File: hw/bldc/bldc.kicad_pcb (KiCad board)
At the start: 2 copper layers, 54 x 29 mm, 71 parts, among them IC1 MP2315SGJ-P, J1 Conn_01x05, J3 Conn_01x06, Q1 BSC13DN30NSFD, Q10 BSC13DN30NSFD, Q2 BSC13DN30NSFD, Q7 BSC13DN30NSFD, Q8 BSC13DN30NSFD, Q9 BSC13DN30NSFD, U1 LD1117S33TR_SOT223, U2 IR2101, U3 IR2101, U4 IR2101, U5 STM32L431CCTx

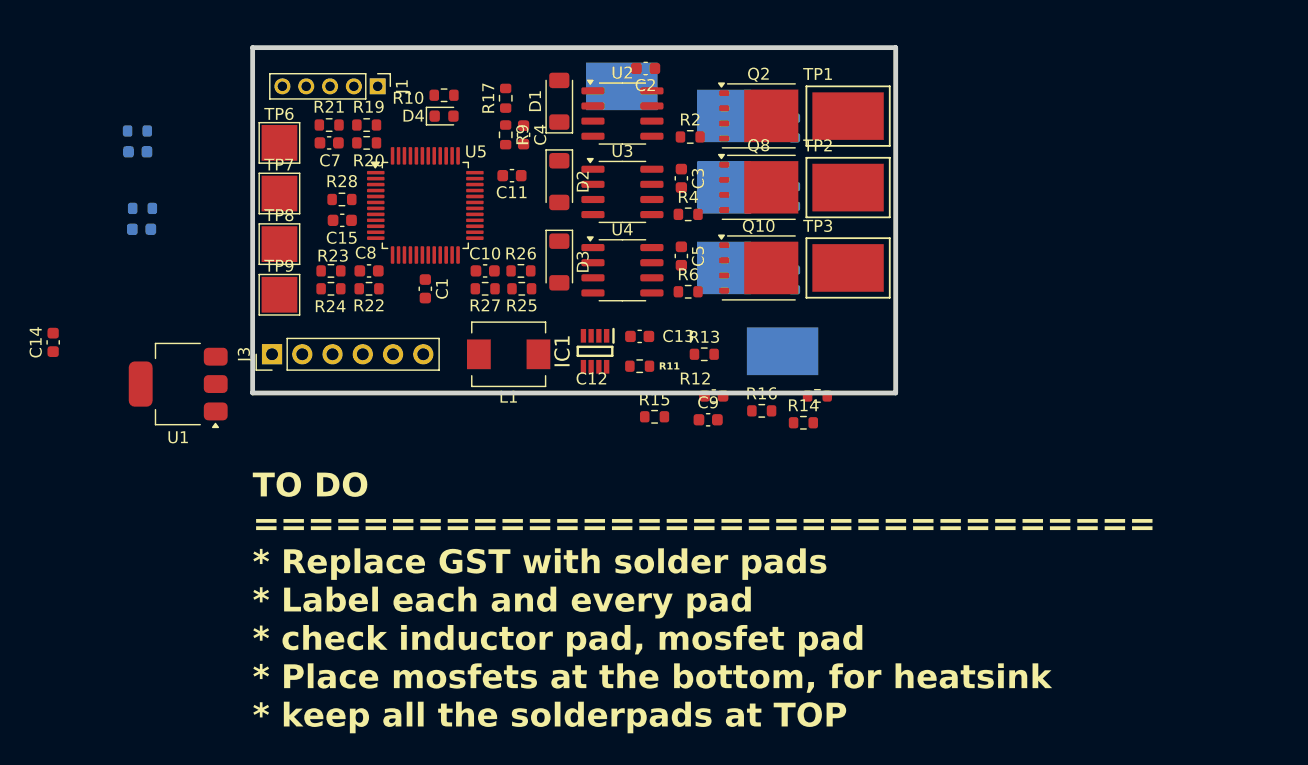
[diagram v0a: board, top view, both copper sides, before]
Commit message: component placement
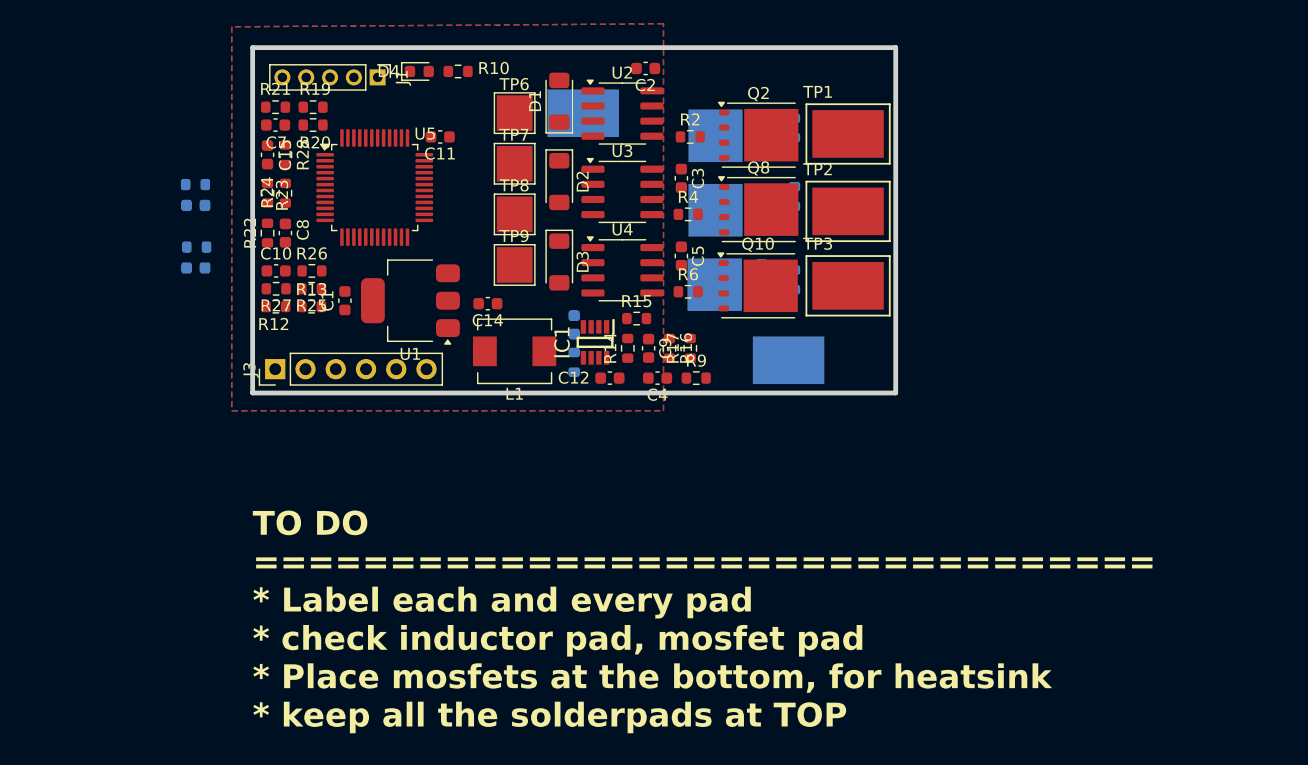
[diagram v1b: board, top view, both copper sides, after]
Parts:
- C13, R11: moved to B.Cu
- C14: value 0.1uF -> 10uF
- moved R12 46.1 mm to (52.0, 117.8)
- moved C14 36.6 mm to (69.8, 117.5), turned to 180 degrees
- moved R13 33.2 mm to (55.0, 117.8)
- moved R17 26.1 mm to (86.8, 121.2)
- moved R9 25.9 mm to (87.2, 123.8), turned to 0 degrees
- moved C4 23.3 mm to (84.0, 123.8), turned to 180 degrees
- moved U1 20.7 mm to (63.2, 117.2)
- moved TP6 19.9 mm to (72.0, 101.5)
- moved TP7 19.9 mm to (72.0, 105.8)
- moved TP8 19.9 mm to (72.0, 110.0)
- moved TP9 19.9 mm to (72.0, 114.2)
- moved R25 17.6 mm to (55.0, 116.2)
- moved C10 17.6 mm to (52.0, 114.8)
- moved R26 17.6 mm to (55.0, 114.8)
- moved R27 17.6 mm to (52.0, 116.2)
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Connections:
- R16 pad 1: VDD -> VDC
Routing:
- added copper zone on B.Cu, net GND
- added copper zone on F.Cu, net GND
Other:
- board text added: "TO DO ================================= * Label each and every pad * check inductor pad, mosfet pad * Place mosfets at the bottom, for heatsink * keep all the solderpads at TOP"
- board text removed: "TO DO ================================= * Replace GST with solder pads * Label each and every pad * check inductor pad, mosfet pad * Place mosfets at the bottom, for heatsink * keep all the solderpads at TOP"

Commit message: pcb routing update
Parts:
- D1, D2, D3: moved to B.Cu
- moved R12 20.6 mm to (72.5, 117.5)
- moved R13 20.6 mm to (75.5, 117.5)
- moved D1 6.05 mm to (81.0, 97.5), turned to 180 degrees
- moved C16 5.52 mm to (45.7, 103.8)
- moved C17 5.52 mm to (45.7, 109.0)
- moved R18 5.52 mm to (45.8, 107.2)
- moved R7 5.52 mm to (45.7, 102.0)
- moved D2 5.30 mm to (81.0, 106.5), turned to 180 degrees
- moved D3 5.30 mm to (81.0, 113.2), turned to 180 degrees
- moved C13 4.49 mm to (74.5, 123.0), turned to 180 degrees
- moved C2 4.07 mm to (85.8, 100.8), turned to -90 degrees
- moved R3 3.26 mm to (95.2, 111.8), turned to 180 degrees
- moved TP6 3.25 mm to (72.0, 98.2)
- moved R1 2.76 mm to (95.2, 105.5), turned to 180 degrees
- moved R5 2.25 mm to (95.5, 117.8), turned to 180 degrees
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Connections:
- U2 pad 2: /TIM1_CH1 -> /TIM1_CH3
- U2 pad 3: /TIM1_CH1N -> /TIM1_CH3N
- U4 pad 2: /TIM1_CH3 -> /TIM1_CH1
- U4 pad 3: /TIM1_CH3N -> /TIM1_CH1N
- U5 pad 28: /LED -> unconnected-(U5-PB15-Pad28)
- U5 pad 32: unconnected-(U5-PA11-Pad32) -> /LED
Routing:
- net +3V3: track 0.00 -> 69.6 mm, vias 0 -> 4
- net /PHASE_A: track 0.00 -> 62.6 mm, vias 0 -> 11
- net /PHASE_B: track 0.00 -> 53.7 mm, vias 0 -> 10
- net /PHASE_C: track 0.00 -> 52.8 mm, vias 0 -> 11
- net VDD: track 0.00 -> 51.7 mm, vias 0 -> 4
- net /ADC_VDC: track 0.00 -> 40.6 mm, vias 0 -> 2
- net /TIM1_CH3N: track 0.00 -> 27.6 mm, vias 0 -> 2
- net /ADC_CENTER: track 0.00 -> 26.5 mm, vias 0 -> 4
- net Net-(U4-HO): track 0.00 -> 23.2 mm, vias 0 -> 1
- net /TIM1_CH2N: track 0.00 -> 22.8 mm, vias 0 -> 2
- net /MCU_TX: track 0.00 -> 22.4 mm, vias 0 -> 1
- net Net-(U3-HO): track 0.00 -> 22.2 mm, vias 0 -> 1
- net /TIM1_CH1N: track 0.00 -> 22.0 mm
- net /MCU_RX: track 0.00 -> 22.0 mm, vias 0 -> 1
- net Net-(U2-HO): track 0.00 -> 21.6 mm, vias 0 -> 1
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- added copper zone on B.Cu, net /PHASE_A
- added copper zone on F.Cu, net /PHASE_A
- added copper zone on B.Cu, net /PHASE_B
- added copper zone on F.Cu, net /PHASE_B
- added copper zone on B.Cu, net /PHASE_C
- added copper zone on F.Cu, net /PHASE_C
- added copper zone on B.Cu, net VDC

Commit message: PCB update
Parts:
- moved C17 29.9 mm to (75.5, 106.5), turned to -90 degrees
- moved R7 21.8 mm to (67.2, 105.5), turned to 0 degrees
- moved R18 21.7 mm to (67.2, 104.0), turned to 0 degrees
- moved C16 21.6 mm to (67.2, 102.5)
- moved R6 1.52 mm to (86.8, 118.0)
- moved R4 0.75 mm to (86.5, 110.8)
- moved C3 0.50 mm to (85.8, 107.0)
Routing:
- net GND: track 15.4 -> 81.9 mm, vias 12 -> 22
- net /ADC_SPD: track 0.00 -> 13.6 mm, vias 0 -> 1
- net Net-(C17-Pad2): track 0.00 -> 12.8 mm, vias 0 -> 1
- net Net-(R18-Pad2): track 0.00 -> 4.13 mm, vias 0 -> 1
- net /ADC_CENTER: track 26.5 -> 30.4 mm
- net /PHASE_B: track 53.7 -> 57.7 mm, vias 10 -> 13
- net Net-(Q10-G): track 3.29 -> 2.01 mm
- net Net-(U4-LO): track 2.19 -> 2.98 mm
- net Net-(Q8-G): track 3.35 -> 2.63 mm

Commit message: PCB UPDATE
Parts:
- moved TP4 1.50 mm to (93.5, 122.2)
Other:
- board size 54 x 29 mm -> 54 x 29.2 mm
- board text added: "3.3V"
- board text added: "GND"
- board text added: "LED"
- board text added: "PHASE A"
- board text added: "PHASE B"
- board text added: "PHASE C"
- board text added: "RPM"
- board text added: "RX"
- board text added: "SPD"
- board text added: "TX"
- board text added: "VCC"
- board text added: "X"
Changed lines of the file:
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@@
 			(at 0 -2.398 0)
 			(layer "F.SilkS")
+			(hide yes)
 			(effects
 				(font
@@
 			(at 0 -2.398 0)
 			(layer "F.SilkS")
+			(hide yes)
 			(effects
 				(font
@@
 		(tags "Test Point")
 		(property "Reference" "TP3"
-			(at -2.5 -3.5 0)
+			(at 0.25 3.5 0)
 			(layer "F.SilkS")
+			(hide yes)
 			(effects
 				(font
@@
 			(at 0 -2.398 0)
 			(layer "F.SilkS")
+			(hide yes)
 			(effects
 				(font
@@
 		(tags "LED")
 		(property "Reference" "D4"
-			(at -2.575 0 0)
+			(at -0.25 -1.5 0)
 			(layer "F.SilkS")
 			(effects
@@
 		(tags "Test Point")
 		(property "Reference" "TP1"
-			(at -2.5 -3.5 0)
+			(at 0.25 -3.5 0)
 			(layer "F.SilkS")
+			(hide yes)
 			(effects
 				(font
@@
 		(tags "test point SMD pad rectangle square")
 		(property "Reference" "TP6"
-			(at 0 -2.398 0)
+			(at 3.5 0.5 0)
 			(layer "F.SilkS")
+			(hide yes)
 			(effects
 				(font
@@
 		(tags "Through hole pin header THT 1x05 2.00mm single row")
 		(property "Reference" "J1"
-			(at 0 -2.06 90)
+			(at 1 -1.75 180)
 			(layer "F.SilkS")
 			(effects
@@
 		(tags "resistor")
 		(property "Reference" "R10"
-			(at -3 0.25 360)
+			(at 0 -1.5 360)
 			(layer "F.SilkS")
 			(effects
@@
 		(tags "CMS SOT")
 		(property "Reference" "U1"
-			(at 0 -4.5 360)
+			(at 5.25 2.75 360)
 			(layer "F.SilkS")
 			(effects
@@
 		(tags "Test Point")
 		(property "Reference" "TP2"
-			(at -2.5 -3.5 0)
+			(at 0.25 -3.25 0)
 			(layer "F.SilkS")
+			(hide yes)
 			(effects
 				(font
@@
 	(footprint "_MAYANK:SOLDERPAD6x4"
 		(layer "B.Cu")
-		(at 95 122.25 180)
+		(at 93.5 122.25 180)
 		(descr "SMT Test Point- Micro Miniature 5015, http://www.keyelco.com/product-pdf.cfm?p=1353")
 		(tags "Test Point")
@@
 	)
 	(gr_rect
-		(start 50 96)
+		(start 50 95.75)
 		(end 104 125)
 		(stroke
@@
 		(layer "Edge.Cuts")
 	)
+	(gr_text "SPD"
+		(at 74 105 0)
+		(layer "F.SilkS")
+		(effects
+			(font
+				(size 0.7 0.7)
+				(thickness 0.15)
+				(bold yes)
+			)
+			(justify left bottom)
+		)
+	)
+	(gr_text "RX"
+		(at 56.25 120.75 0)
+		(layer "F.SilkS")
+		(effects
+			(font
+				(size 0.7 0.7)
+				(thickness 0.15)
+				(bold yes)
+			)
+			(justify left bottom)
+		)
+	)
+	(gr_text "VCC"
+		(at 59.5 101 0)
+		(layer "F.SilkS")
+		(effects
+			(font
+				(size 0.7 0.7)
+				(thickness 0.15)
+				(bold yes)
+			)
+			(justify left bottom)
+		)
+	)
+	(gr_text "PHASE B"
+		(at 98.25 107 0)
+		(layer "F.SilkS")
+		(effects
+			(font
+				(size 0.7 0.7)
+				(thickness 0.15)
+				(bold yes)
+			)
+			(justify left bottom)
+		)
+	)
+	(gr_text "PHASE A"
+		(at 98.25 100.5 0)
+		(layer "F.SilkS")
+		(effects
+			(font
+				(size 0.7 0.7)
+				(thickness 0.15)
+				(bold yes)
+			)
+			(justify left bottom)
+		)
+	)
+	(gr_text "PHASE C"
+		(at 98.25 113.25 0)
+		(layer "F.SilkS")
+		(effects
+			(font
+				(size 0.7 0.7)
+				(thickness 0.15)
+				(bold yes)
+			)
+			(justify left bottom)
+		)
+	)
+	(gr_text "GND"
+		(at 74 113.5 0)
+		(layer "F.SilkS")
+		(effects
+			(font
+				(size 0.7 0.7)
+				(thickness 0.15)
+				(bold yes)
+			)
+			(justify left bottom)
+		)
+	)
+	(gr_text "X"
+		(at 58.75 120.75 0)
+		(layer "F.SilkS")
+		(effects
+			(font
+				(size 0.7 0.7)
+				(thickness 0.15)
+				(bold yes)
+			)
+			(justify left bottom)
+		)
+	)
+	(gr_text "RPM"
+		(at 74 109.25 0)
+		(layer "F.SilkS")
+		(effects
+			(font
+				(size 0.7 0.7)
+				(thickness 0.15)
+				(bold yes)
+			)
+			(justify left bottom)
+		)
+	)
 	(gr_text "TO DO\n=================================\n* Label each and every pad\n* check inductor pad, mosfet pad\n* Place mosfets at the bottom, for heatsink\n* keep all the solderpads at TOP"
 		(at 50 153.25 0)
@@
 		)
 	)
+	(gr_text "TX"
+		(at 53.5 120.75 0)
+		(layer "F.SilkS")
+		(effects
+			(font
+				(size 0.7 0.7)
+				(thickness 0.15)
+				(bold yes)
+			)
+			(justify left bottom)
+		)
+	)
+	(gr_text "3.3V"
+		(at 74 99 0)
+		(layer "F.SilkS")
+		(effects
+			(font
+				(size 0.7 0.7)
+				(thickness 0.15)
+			)
+			(justify left bottom)
+		)
+	)
+	(gr_text "X"
+		(at 51.25 120.75 0)
+		(layer "F.SilkS")
+		(effects
+			(font
+				(size 0.7 0.7)
+				(thickness 0.15)
+				(bold yes)
+			)
+			(justify left bottom)
+		)
+	)
+	(gr_text "LED"
+		(at 63 99.75 0)
+		(layer "F.SilkS")
+		(effects
+			(font
+				(size 0.7 0.7)
+				(thickness 0.15)
+				(bold yes)
+			)
+			(justify left bottom)
+		)
+	)
 	(segment
 		(start 83.525 99.63)
@@
 		(polygon
 			(pts
-				(xy 91 100.5) (xy 91 105) (xy 91.5 105.5) (xy 103.5 105.5) (xy 103.5 100.25) (xy 91.25 100.25)
+				(xy 91 101.5) (xy 91 105) (xy 91.5 105.5) (xy 103.25 105.5) (xy 103.25 101) (xy 91.5 101)
 			)
 		)
@@
 		(polygon
 			(pts
-				(xy 91.25 113.25) (xy 90.75 113.75) (xy 90.75 118.25) (xy 91.75 118.75) (xy 103 118.75) (xy 103.75 118)
-				(xy 103.75 113.75) (xy 103 113.25)
+				(xy 91.5 113.5) (xy 91 114) (xy 91 118) (xy 91.75 118.5) (xy 103 118.5) (xy 103.5 118) (xy 103.5 114)
+				(xy 103 113.5)
 			)
 		)
@@
 		(polygon
 			(pts
-				(xy 91.75 106.75) (xy 90.75 107.5) (xy 90.75 112) (xy 91.5 112) (xy 102.75 112) (xy 103.5 112) (xy 103.5 107.25)
-				(xy 103 106.75)
+				(xy 91.25 107.25) (xy 90.75 107.75) (xy 90.75 112) (xy 91.5 112) (xy 102.75 112) (xy 103.25 112)
+				(xy 103.25 107.75) (xy 102.5 107.25)
 			)
 		)
@@
 		(polygon
 			(pts
-				(xy 48.25 94.25) (xy 48.25 126.5) (xy 84.5 126.5) (xy 84.5 94)
+				(xy 50 95.75) (xy 50 125) (xy 84.5 125) (xy 84.5 95.75)
 			)
 		)
@@
 			(pts
 				(xy 91.75 123.75) (xy 86.25 118.5) (xy 86.25 100.5) (xy 86.75 100) (xy 90.75 100) (xy 91.25 100.5)
-				(xy 91.25 118) (xy 93.25 120) (xy 98 120) (xy 98.5 120.5) (xy 98.5 123.75) (xy 98 124.25) (xy 92.25 124.25)
+				(xy 91.25 118) (xy 93.25 120) (xy 96.75 120) (xy 97.25 120.5) (xy 97.25 123.75) (xy 96.75 124.25)
+				(xy 92.25 124.25)
 			)
 		)
